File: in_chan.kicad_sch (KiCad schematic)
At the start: 7 parts, among them U7 MAX31910AUI+

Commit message: fix warnings
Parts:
- renumbered C41 to C45, C42 to C46, C43 to C47, C44 to C48, R4 to R10, R5 to R11, U7 to U8
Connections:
- net GNDPWR: now also U8.25 (CLK), U8.27 (SIN); no longer U8.28 (GND)
- net INPWR: now also U8.24 (*CS); no longer U8.14 (VCC24V)

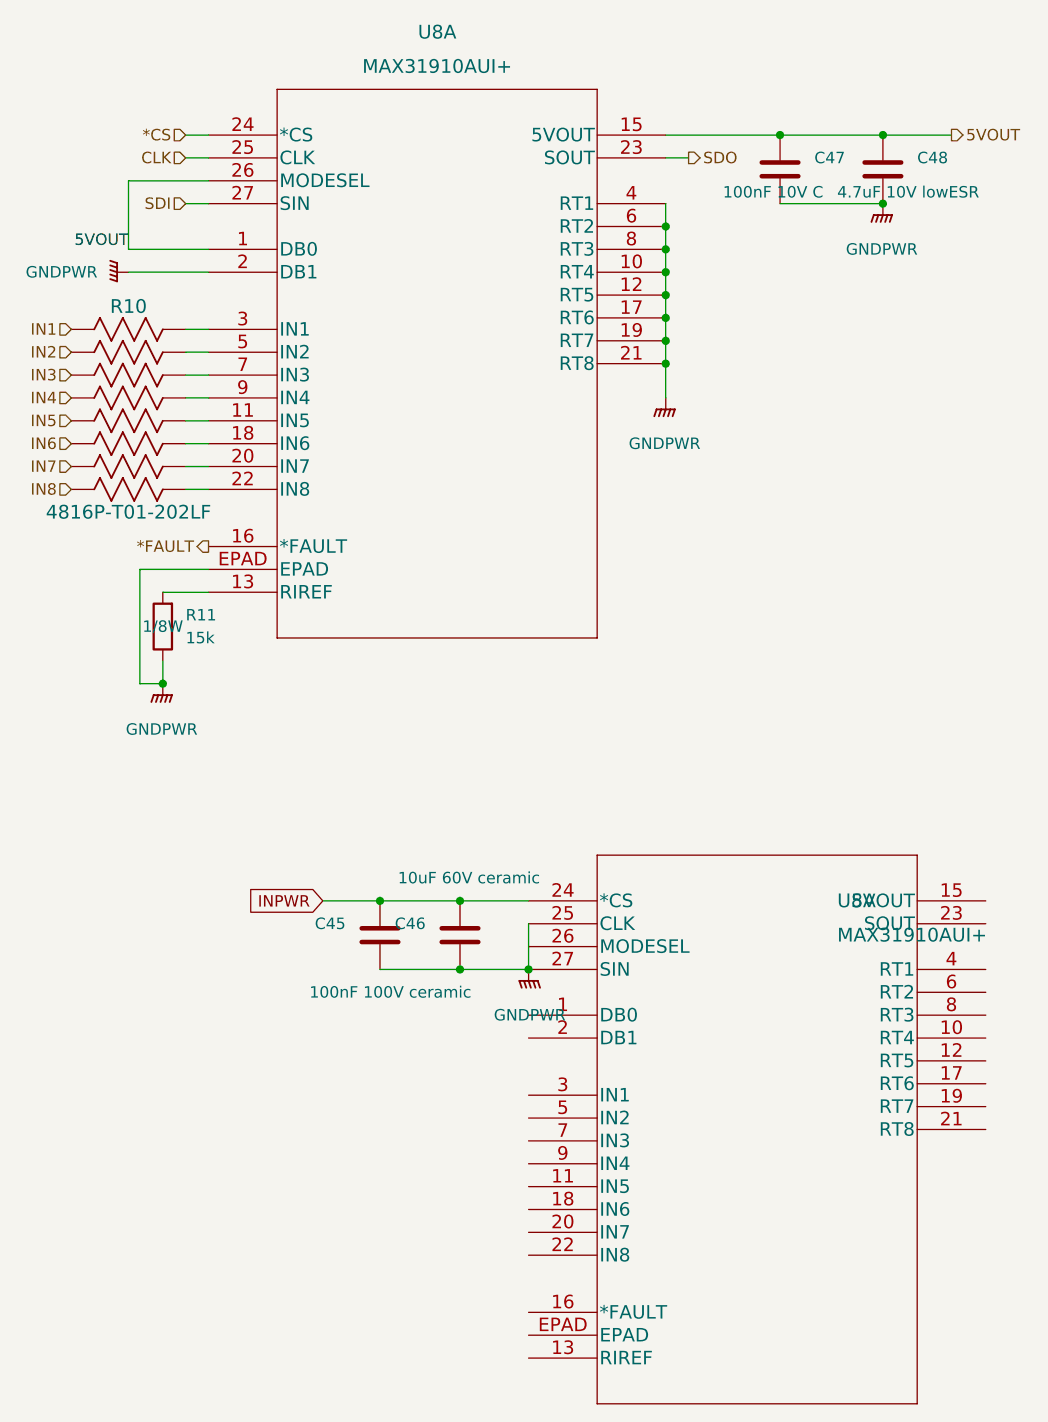
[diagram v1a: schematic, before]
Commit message: move MPG to dedicated file
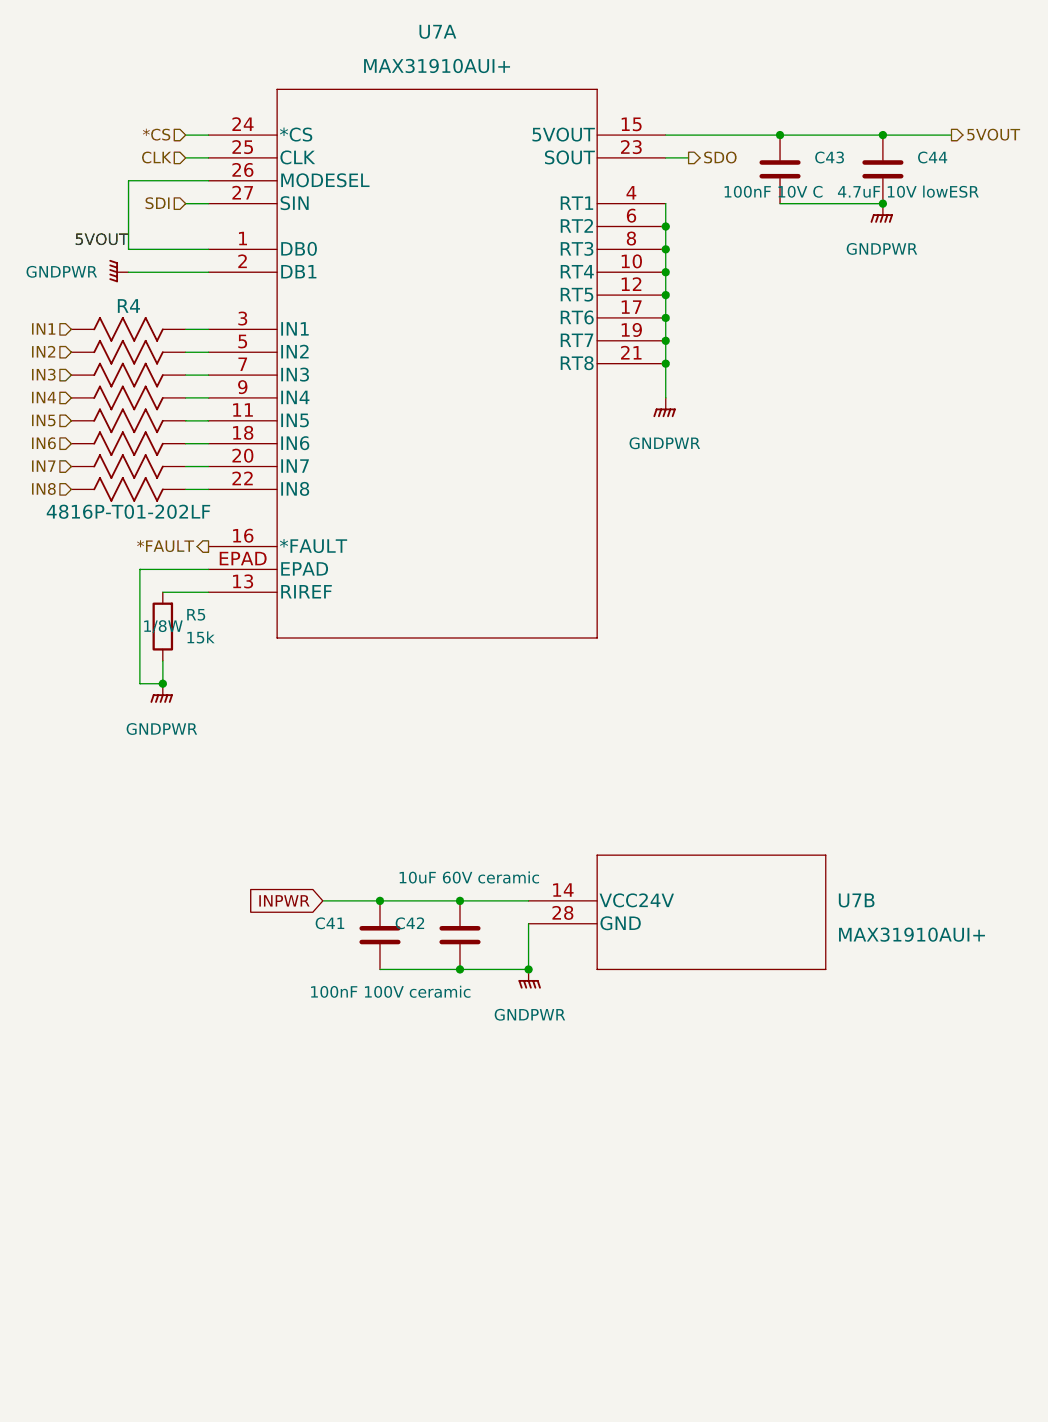
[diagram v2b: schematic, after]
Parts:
- renumbered C45 to C41, C46 to C42, C47 to C43, C48 to C44, R10 to R4, R11 to R5, U8 to U7
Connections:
- net GNDPWR: now also U7.28 (GND); no longer U7.25 (CLK), U7.27 (SIN)
- net INPWR: now also U7.14 (VCC24V); no longer U7.24 (*CS)
